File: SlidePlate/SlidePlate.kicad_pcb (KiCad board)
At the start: 2 copper layers, 56 x 100 mm, 10 parts, among them J1 Conn_01x01, J2 Conn_01x01, J3 Conn_01x01, J4 Conn_01x01

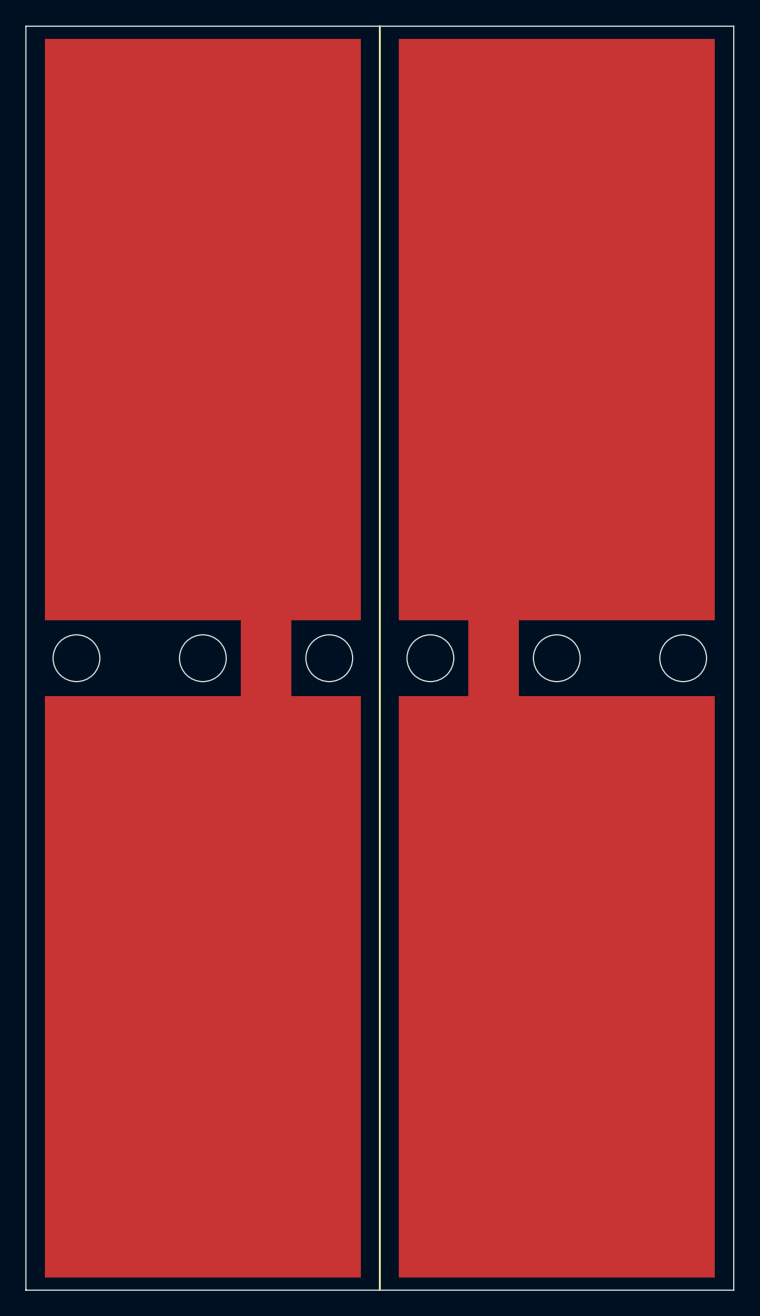
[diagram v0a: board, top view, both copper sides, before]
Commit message: Added more ruled lines
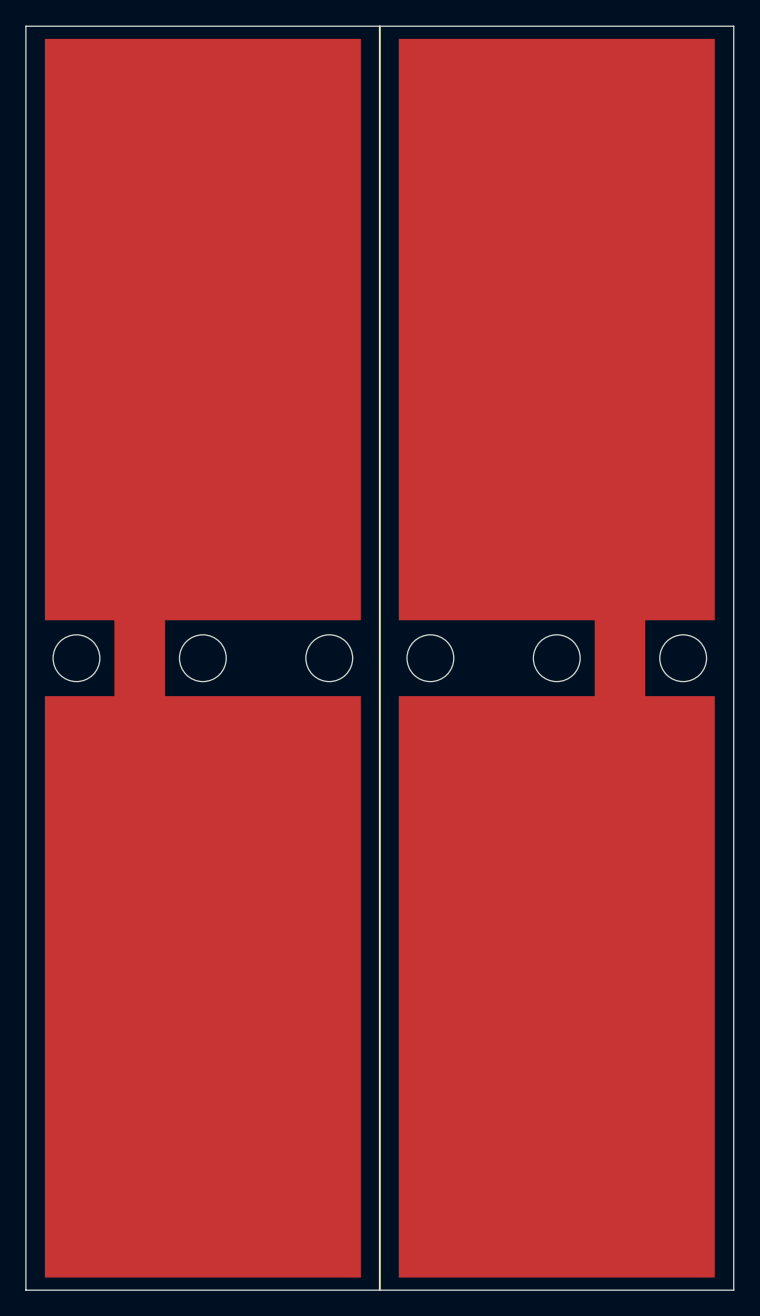
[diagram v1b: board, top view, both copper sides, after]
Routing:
- net Net-(J2-Pad1): track 60.4 -> 74.5 mm
- net Net-(J1-Pad1): track 60.4 -> 74.5 mm
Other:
- board text added: "0"
- board text added: "1"
- board text added: "10"
- board text added: "11"
- board text added: "12"
- board text added: "2"
- board text added: "3"
- board text added: "4"
- board text added: "5"
- board text added: "6"
- board text added: "7"
- board text added: "8"
- board text added: "9"

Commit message: Modified resistive bridge
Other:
- board text added: "SLIDE PLATE BY DANIEL MARKS KW4TI CC-BY-SA 4.0"
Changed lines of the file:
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@@
+    (effects (font (size 1 1) (thickness 0.15)) (justify mirror))
+  )
+  (gr_text "SLIDE PLATE BY DANIEL MARKS KW4TI CC-BY-SA 4.0" (at 75 43 90) (layer "B.SilkS")
     (effects (font (size 1 1) (thickness 0.15)) (justify mirror))
   )
@@
     (effects (font (size 1 1) (thickness 0.15)) (justify mirror))
   )
+  (gr_text "SLIDE PLATE BY DANIEL MARKS KW4TI CC-BY-SA 4.0" (at 21 43 90) (layer "B.SilkS")
+    (effects (font (size 1 1) (thickness 0.15)) (justify mirror))
+  )
